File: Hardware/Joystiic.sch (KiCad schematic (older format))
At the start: 11 parts, among them J1 Qwiic_Connector, J2 Qwiic_Connector, J3 I2C_Standard_PTH_Connector, J4 AVR_SPI_PROG_3X2TESTPOINTS, U1 ATTINY85-20SU

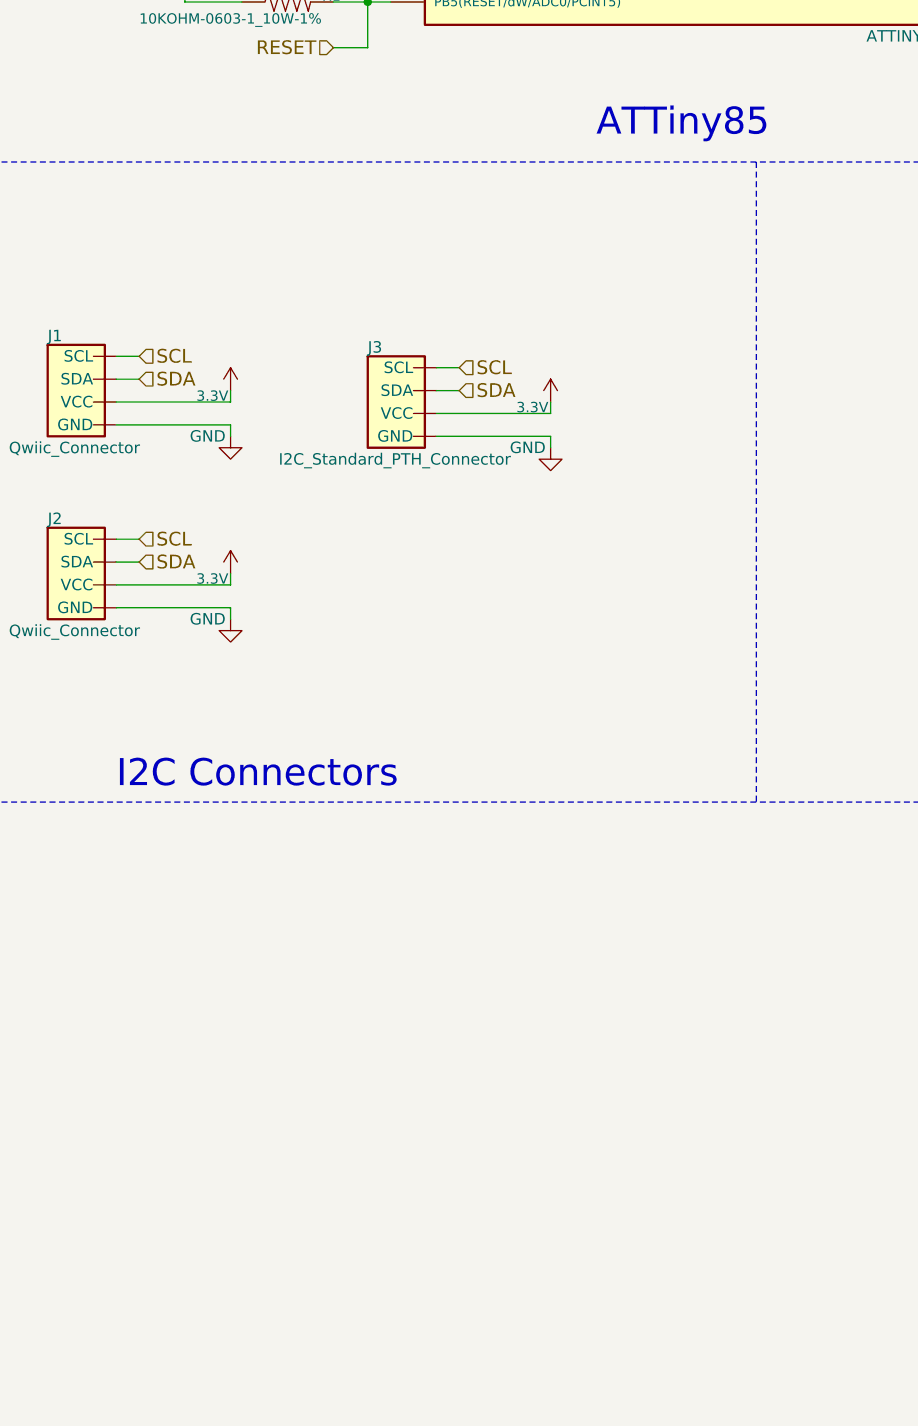
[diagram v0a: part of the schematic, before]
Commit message: v1.1
- Buzzard Silkscreen
- Wide SOIC footprint
- Power LED
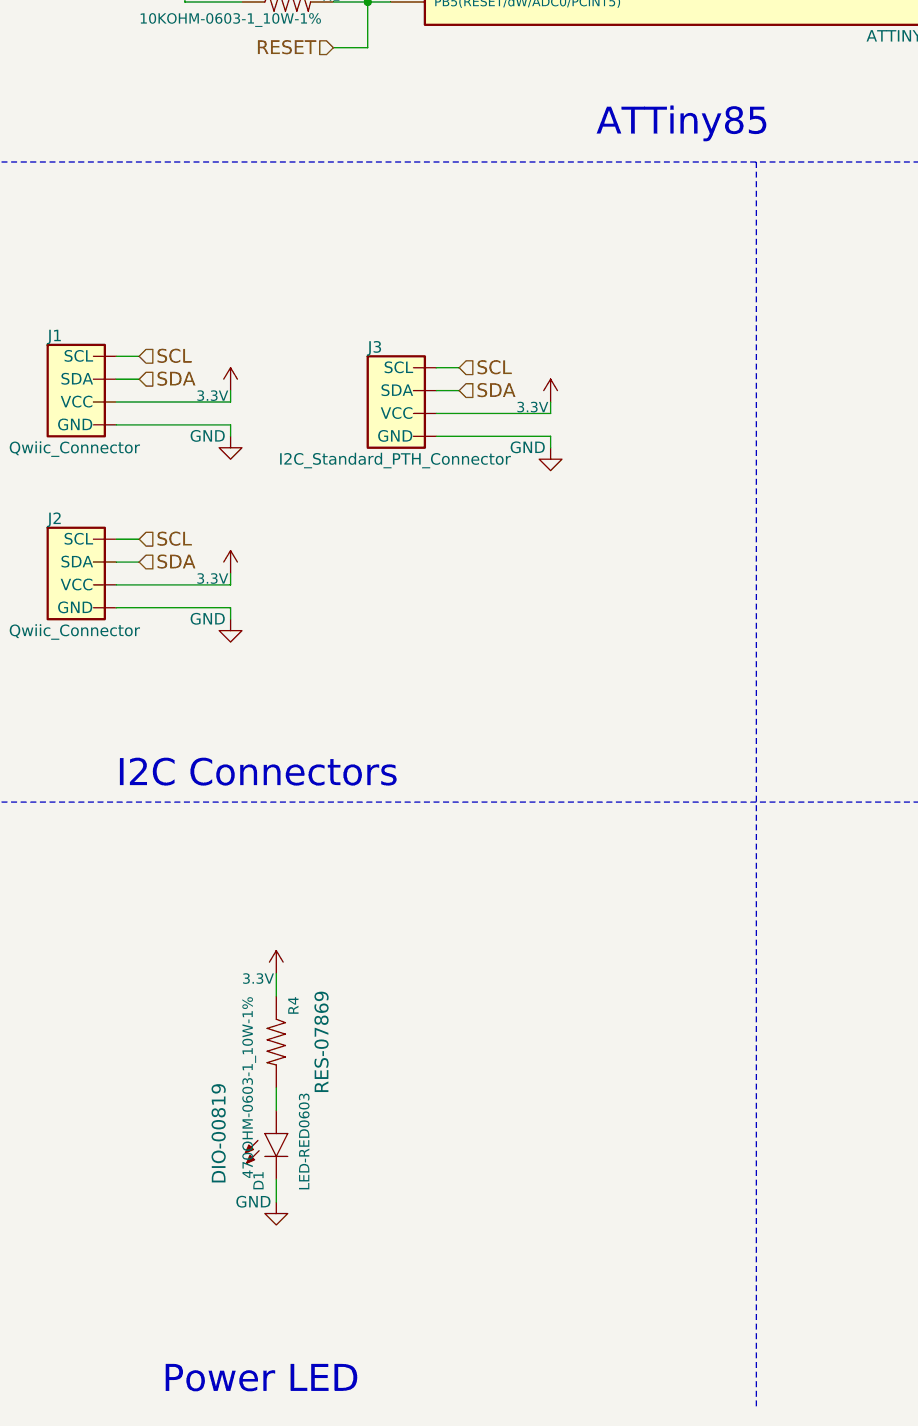
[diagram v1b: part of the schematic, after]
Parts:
- added D1: LED-RED0603, LED:LED-0603, symbol LED-RED0603
- added R4: 470OHM-0603-1_10W-1%, Resistors:0603, symbol 470OHM-0603-1_10W-1%
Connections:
- net 3.3V: now also R4.1
- net GND: now also D1.C
- new net: D1.A, R4.2
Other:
- note added: "Power LED\n"
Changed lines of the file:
@@
 	450  5150 11200 5150
 Wire Notes Line
-	4550 2350 4550 5150
+	4550 2350 4550 7800
 Wire Notes Line
 	8200 500  8200 5150
@@
 Text Notes 8750 5100 0    118  ~ 0
 I2C Pullup Jumper
+Text Notes 1950 7750 0    118  ~ 0
+Power LED\n
+$Comp
+L GND #PWR018
+U 1 1 5A8DEFDE
+P 2450 6900
+F 0 "#PWR018" H 2450 6650 50  0001 C CNN
+F 1 "GND" H 2350 6900 50  0000 C CNN
+F 2 "" H 2450 6900 50  0001 C CNN
+F 3 "" H 2450 6900 50  0001 C CNN
+	1    2450 6900
+	1    0    0    -1
+$EndComp
+$Comp
+L 3.3V #SUPPLY019
+U 1 1 5A8DF00A
+P 2450 5900
+F 0 "#SUPPLY019" H 2500 5900 45  0001 L BNN
+F 1 "3.3V" H 2300 5850 45  0000 L BNN
+F 2 "XXX-00000" H 2450 6200 60  0001 C CNN
+F 3 "" H 2450 5900 60  0001 C CNN
+	1    2450 5900
+	1    0    0    -1
+$EndComp
+$Comp
+L 470OHM-0603-1_10W-1% R4
+U 1 1 5A8DF723
+P 2450 6200
+F 0 "R4" H 2250 6250 45  0000 L BNN
+F 1 "470OHM-0603-1_10W-1%" H 2250 6050 45  0000 L BNN
+F 2 "Resistors:0603" H 2450 6350 20  0001 C CNN
+F 3 "" H 2450 6200 60  0001 C CNN
+F 4 "RES-07869" H 2450 6400 60  0000 C CNN "Field4"
+	1    2450 6200
+	0    1    1    0
+$EndComp
+$Comp
+L LED-RED0603 D1
+U 1 1 5A8DF783
+P 2450 6600
+F 0 "D1" V 2400 6350 45  0000 L BNN
+F 1 "LED-RED0603" V 2600 6350 45  0000 L BNN
+F 2 "LED:LED-0603" V 2250 6600 20  0001 C CNN
+F 3 "" H 2450 6600 50  0001 C CNN
+F 4 "DIO-00819" V 2200 6600 60  0000 C CNN "Field4"
+	1    2450 6600
+	1    0    0    -1
+$EndComp
+Wire Wire Line
+	2450 5900 2450 6000
+Wire Wire Line
+	2450 6400 2450 6500
+Wire Wire Line
+	2450 6800 2450 6900
 $EndSCHEMATC
